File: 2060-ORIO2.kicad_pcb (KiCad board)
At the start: 4 copper layers, 100 x 100 mm, 196 parts, among them J11 RaspberryPI-B+header, J12 Conn_01x04, J13 Conn_01x08, J14 Conn_01x02, J15 Conn_01x08, J16 Conn_01x10, J17 Conn_01x10, J18 Conn_01x10, J19 Conn_01x10, J20 Conn_01x09, J21 Conn_01x08, J22 Conn_01x08, J23 Conn_01x08, J24 Conn_01x08, J25 Conn_01x08, J26 Conn_01x08, J27 Conn_01x02, J28 Conn_01x16, J29 Conn_01x16, J30 Conn_01x16, J31 Conn_01x08, J32 Conn_01x08, J33 Conn_01x08, J34 Conn_01x08, J35 TBL001-500-02GY-2GY, Q11 ULN2803ADWR, Q12 BCV27, SW11 SW_DIP_x08, U11 ICE40HX4K-TQ144, U12 SN74LVC4245AN, U13 SN74LVC4245AN, U14 SN74LVC4245AN, U15 TPS563231, U16 MCP3008, U17 AZ1117CH-3.3TRG1, U18 AZ1117CH-3.3TRG1, U19 AZ1117CH-1.2, U20 TPS563231, U21 SN74LVC4245AN, U22 SN74LVC4245AN, U23 SN74LVC4245AN, U24 SN74LVC4245AN, U25 TPS563231, U26 AP3012, Y11 XLH536025_000000I

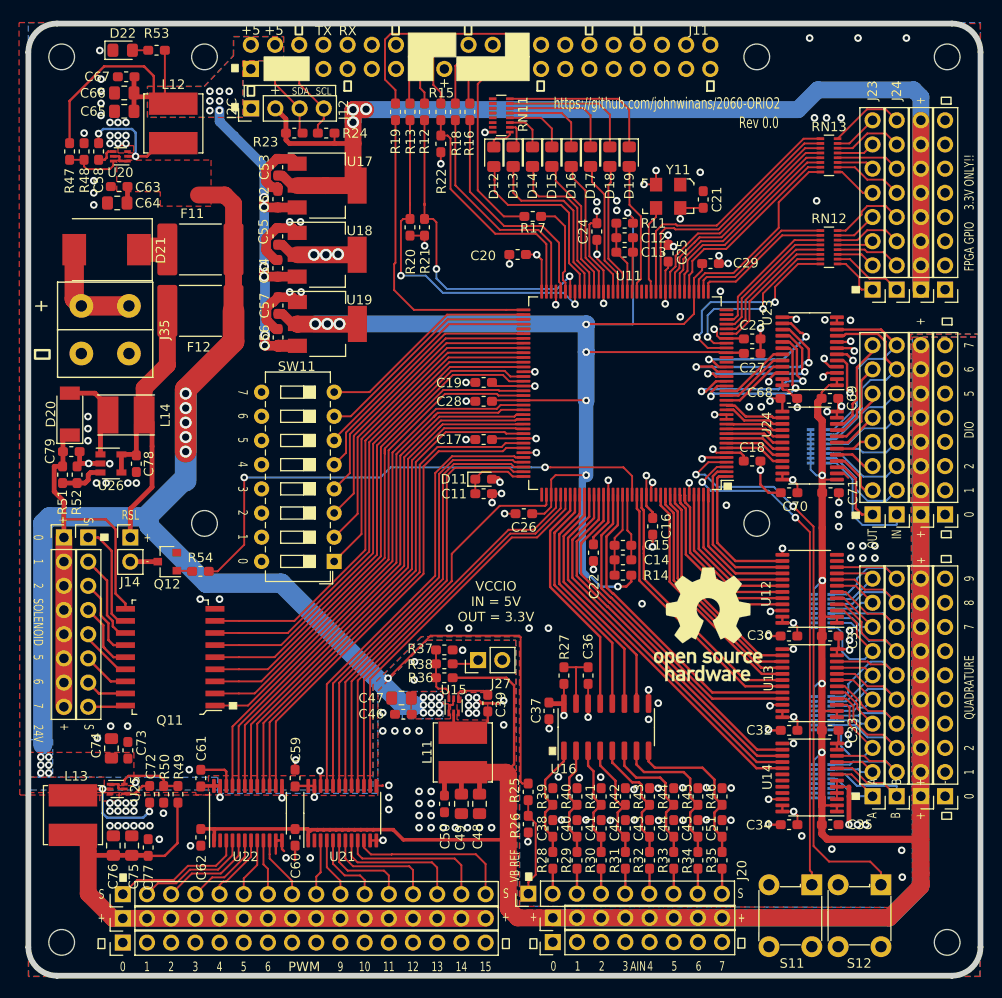
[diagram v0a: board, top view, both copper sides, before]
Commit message: Cosmetic silkscreen changes.
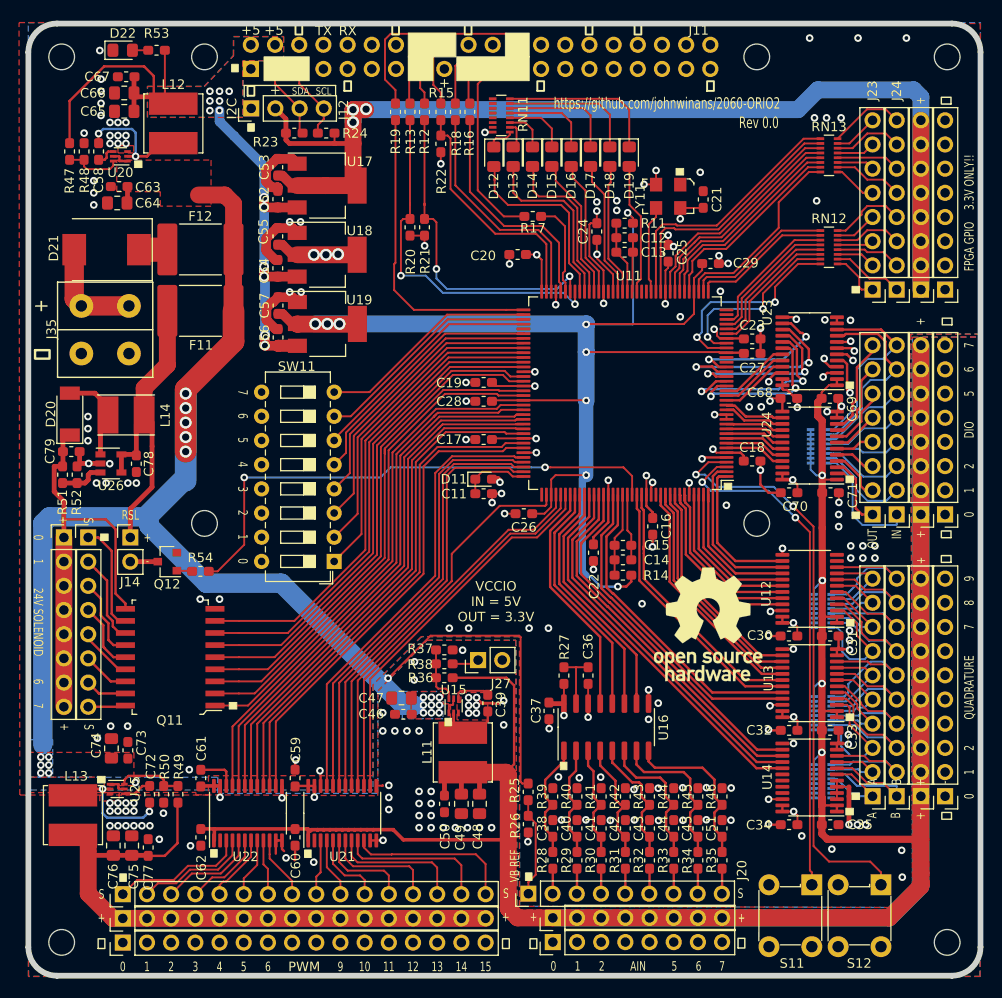
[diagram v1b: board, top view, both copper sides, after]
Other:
- board text added: "24V SOLENOID"
- board text removed: "24V"
- board text removed: "SOLENOID"
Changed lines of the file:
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@@
   (general
     (thickness 1.6)
-    (drawings 159)
+    (drawings 165)
     (tracks 2365)
     (zones 0)
@@
     (visible_elements FFFFFF7F)
     (pcbplotparams
-      (layerselection 0x010f8_ffffffff)
+      (layerselection 0x010f0_ffffffff)
       (usegerberextensions false)
       (usegerberattributes false)
@@
       (psa4output false)
       (plotreference true)
-      (plotvalue true)
+      (plotvalue false)
       (plotinvisibletext false)
       (padsonsilk false)
@@
     (tags "resistor handsolder")
     (attr smd)
-    (fp_text reference F12 (at 0.1778 -10.2616) (layer F.SilkS)
+    (fp_text reference F12 (at 0.0127 3.4798) (layer F.SilkS)
       (effects (font (size 1 1) (thickness 0.15)))
     )
@@
     (tags "resistor handsolder")
     (attr smd)
-    (fp_text reference F11 (at -0.8636 -10.2108) (layer F.SilkS)
+    (fp_text reference F11 (at 0.0508 3.6068) (layer F.SilkS)
       (effects (font (size 1 1) (thickness 0.15)))
     )
@@
     (tags "capacitor handsolder")
     (attr smd)
-    (fp_text reference C71 (at 2.3551 -0.0254 90) (layer F.SilkS)
+    (fp_text reference C71 (at 2.3297 0.2794 90) (layer F.SilkS)
       (effects (font (size 1 1) (thickness 0.15)))
     )
@@
     (tags "capacitor handsolder")
     (attr smd)
-    (fp_text reference C69 (at 2.3175 -0.0254 90) (layer F.SilkS)
+    (fp_text reference C69 (at 2.3175 1.1049 90) (layer F.SilkS)
       (effects (font (size 1 1) (thickness 0.15)))
     )
@@
     (tags "capacitor handsolder")
     (attr smd)
-    (fp_text reference C33 (at 2.3622 -0.0127 270) (layer F.SilkS)
+    (fp_text reference C33 (at 2.3241 0.6858 270) (layer F.SilkS)
       (effects (font (size 1 1) (thickness 0.15)))
     )
@@
     (tags "capacitor handsolder")
     (attr smd)
-    (fp_text reference C31 (at 2.3622 0.0381 90) (layer F.SilkS)
+    (fp_text reference C31 (at 2.3495 0.7493 90) (layer F.SilkS)
       (effects (font (size 1 1) (thickness 0.15)))
     )
@@
   (module jb-footprint:TBL001-500-02GY-2GY (layer F.Cu)
     (at 80.0658 74.1564 90)
-    (fp_text reference J35 (at 0 6.2484 270) (layer F.SilkS)
+    (fp_text reference J35 (at 0.0635 -5.6388 270) (layer F.SilkS)
       (effects (font (size 1 1) (thickness 0.15)))
     )
@@
     (tags "Diode SMC (DO-214AB)")
     (attr smd)
-    (fp_text reference D21 (at -5.6896 -0.0762 270) (layer F.SilkS)
+    (fp_text reference D21 (at 5.5499 0.1524 270) (layer F.SilkS)
       (effects (font (size 1 1) (thickness 0.15)))
     )
@@
     (at 140.467 59.018 180)
     (attr smd)
-    (fp_text reference Y11 (at 0.2286 1.651 180) (layer F.SilkS)
+    (fp_text reference Y11 (at 4.2037 -1.143 270) (layer F.SilkS)
       (effects (font (size 1 1) (thickness 0.15)))
     )
@@
     (tags "SOIC SO")
     (attr smd)
-    (fp_text reference U16 (at -4.3803 -4.4963 180) (layer F.SilkS)
+    (fp_text reference U16 (at -0.0369 6.0193 270) (layer F.SilkS)
       (effects (font (size 1 1) (thickness 0.15)))
     )
@@
     )
   )
+  (gr_poly (pts (xy 116.4528 114.9615) (xy 116.4528 115.7615) (xy 115.7528 115.7615) (xy 115.7528 114.9615)) (layer F.SilkS) (width 0.1))
+  (gr_poly (pts (xy 101.7081 128.7918) (xy 101.7081 129.5918) (xy 101.0081 129.5918) (xy 101.0081 128.7918)) (layer F.SilkS) (width 0.1))
+  (gr_poly (pts (xy 91.8402 128.7538) (xy 91.8402 129.5538) (xy 91.1402 129.5538) (xy 91.1402 128.7538)) (layer F.SilkS) (width 0.1))
+  (gr_poly (pts (xy 80.0658 121.7575) (xy 79.2658 121.7575) (xy 79.2658 121.0575) (xy 80.0658 121.0575)) (layer F.SilkS) (width 0.1))
+  (gr_poly (pts (xy 83.9393 57.1272) (xy 83.1393 57.1272) (xy 83.1393 56.4272) (xy 83.9393 56.4272)) (layer F.SilkS) (width 0.1))
+  (gr_poly (pts (xy 140.8226 57.9146) (xy 140.0226 57.9146) (xy 140.0226 57.2146) (xy 140.8226 57.2146)) (layer F.SilkS) (width 0.1))
+  (gr_poly (pts (xy 158.6534 125.1103) (xy 157.8534 125.1103) (xy 157.8534 124.4103) (xy 158.6534 124.4103)) (layer F.SilkS) (width 0.1))
+  (gr_poly (pts (xy 158.6788 115.2043) (xy 157.8788 115.2043) (xy 157.8788 114.5043) (xy 158.6788 114.5043)) (layer F.SilkS) (width 0.1))
+  (gr_poly (pts (xy 158.7169 105.2856) (xy 157.9169 105.2856) (xy 157.9169 104.5856) (xy 158.7169 104.5856)) (layer F.SilkS) (width 0.1))
+  (gr_poly (pts (xy 158.6661 90.2234) (xy 157.8661 90.2234) (xy 157.8661 89.5234) (xy 158.6661 89.5234)) (layer F.SilkS) (width 0.1))
+  (gr_poly (pts (xy 158.6788 80.3428) (xy 157.8788 80.3428) (xy 157.8788 79.6428) (xy 158.6788 79.6428)) (layer F.SilkS) (width 0.1))
   (gr_text RSL (at 82.7074 93.6382) (layer F.SilkS)
     (effects (font (size 1 0.7) (thickness 0.15)))
@@
   (gr_line (start 104.272 48.5024) (end 94.6708 48.5024) (layer F.SilkS) (width 0.12))
   (gr_line (start 104.272 49.5438) (end 104.272 48.5024) (layer F.SilkS) (width 0.12))
-  (gr_poly (pts (xy 94.05 50.382) (xy 94.05 51.182) (xy 93.35 51.182) (xy 93.35 50.382)) (layer F.SilkS) (width 0.1))
+  (gr_poly (pts (xy 95.7376 52.5157) (xy 95.7376 53.3157) (xy 95.0376 53.3157) (xy 95.0376 52.5157)) (layer F.SilkS) (width 0.1))
   (gr_text "Rev 0.0" (at 116.9212 53.3284) (layer B.SilkS)
     (effects (font (size 1.2 0.8) (thickness 0.2)) (justify mirror))
@@
     (effects (font (size 1.2 0.8) (thickness 0.2)) (justify mirror))
   )
-  (gr_text 24V (at 73.03 116.565 270) (layer F.SilkS)
-    (effects (font (size 1 0.7) (thickness 0.15)))
-  )
   (gr_poly (pts (xy 124.9 131.2) (xy 124.9 132) (xy 124.2 132) (xy 124.2 131.2)) (layer F.SilkS) (width 0.1))
   (gr_text 6 (at 94.5092 83.2153 270) (layer F.SilkS)
@@
   )
   (gr_poly (pts (xy 93.896 114) (xy 93.096 114) (xy 93.096 113.3) (xy 93.896 113.3)) (layer F.SilkS) (width 0.1))
-  (gr_poly (pts (xy 127.4 118) (xy 127.4 118.8) (xy 126.7 118.8) (xy 126.7 118)) (layer F.SilkS) (width 0.1))
-  (gr_poly (pts (xy 145.85 90.95) (xy 145.05 90.95) (xy 145.05 90.25) (xy 145.85 90.25)) (layer F.SilkS) (width 0.1))
+  (gr_poly (pts (xy 128.5686 119.5717) (xy 128.5686 120.3717) (xy 127.8686 120.3717) (xy 127.8686 119.5717)) (layer F.SilkS) (width 0.1))
+  (gr_poly (pts (xy 145.8772 90.9727) (xy 145.0772 90.9727) (xy 145.0772 90.2727) (xy 145.8772 90.2727)) (layer F.SilkS) (width 0.1))
   (gr_poly (pts (xy 94.05 46.28) (xy 94.05 47.08) (xy 93.35 47.08) (xy 93.35 46.28)) (layer F.SilkS) (width 0.1))
   (gr_poly (pts (xy 80.3854 96.3) (xy 79.5854 96.3) (xy 79.5854 95.6) (xy 80.3854 95.6)) (layer F.SilkS) (width 0.1))
@@
     (effects (font (size 1.016 1.016) (thickness 0.2032)))
   )
-  (gr_text 3 (at 134.7012 141.0092) (layer F.SilkS)
-    (effects (font (size 1 0.7) (thickness 0.15)))
-  )
   (gr_text 7 (at 144.8612 141.0092) (layer F.SilkS)
     (effects (font (size 1 0.7) (thickness 0.15)))
@@
     (effects (font (size 1 0.7) (thickness 0.15)))
   )
-  (gr_text 4 (at 137.3047 141.0092) (layer F.SilkS)
-    (effects (font (size 1 0.7) (thickness 0.15)))
-  )
   (gr_text 5 (at 139.8447 141.0092) (layer F.SilkS)
     (effects (font (size 1 0.7) (thickness 0.15)))
@@
     (effects (font (size 1 0.7) (thickness 0.15)))
   )
-  (gr_text 5 (at 73.03 108.5734 270) (layer F.SilkS)
-    (effects (font (size 1 0.7) (thickness 0.15)))
-  )
-  (gr_text SOLENOID (at 73.03 104.865 270) (layer F.SilkS)
-    (effects (font (size 1 0.7) (thickness 0.15)))
-  )
-  (gr_text 2 (at 73.03 101.055 270) (layer F.SilkS)
+  (gr_text "24V SOLENOID" (at 73.03 104.865 270) (layer F.SilkS)
     (effects (font (size 1 0.7) (thickness 0.15)))
   )
@@
   (segment (start 92.7895 120.5605) (end 92.602 120.373) (width 0.254) (layer F.Cu) (net 1))
   (segment (start 107.8955 127.7935) (end 108.5455 127.7935) (width 0.254) (layer F.Cu) (net 1))
-  (via (at 101.605 129.63) (size 0.8) (drill 0.4) (layers F.Cu B.Cu) (net 1))
+  (via (at 101.9733 130.0745) (size 0.8) (drill 0.4) (layers F.Cu B.Cu) (net 1))
   (segment (start 100.0175 128.9175) (end 100.0175 129.8205) (width 0.254) (layer F.Cu) (net 1))
   (segment (start 100.0175 129.8205) (end 99.954 129.884) (width 0.254) (layer F.Cu) (net 1))

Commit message: Change regulators & add current limiters.
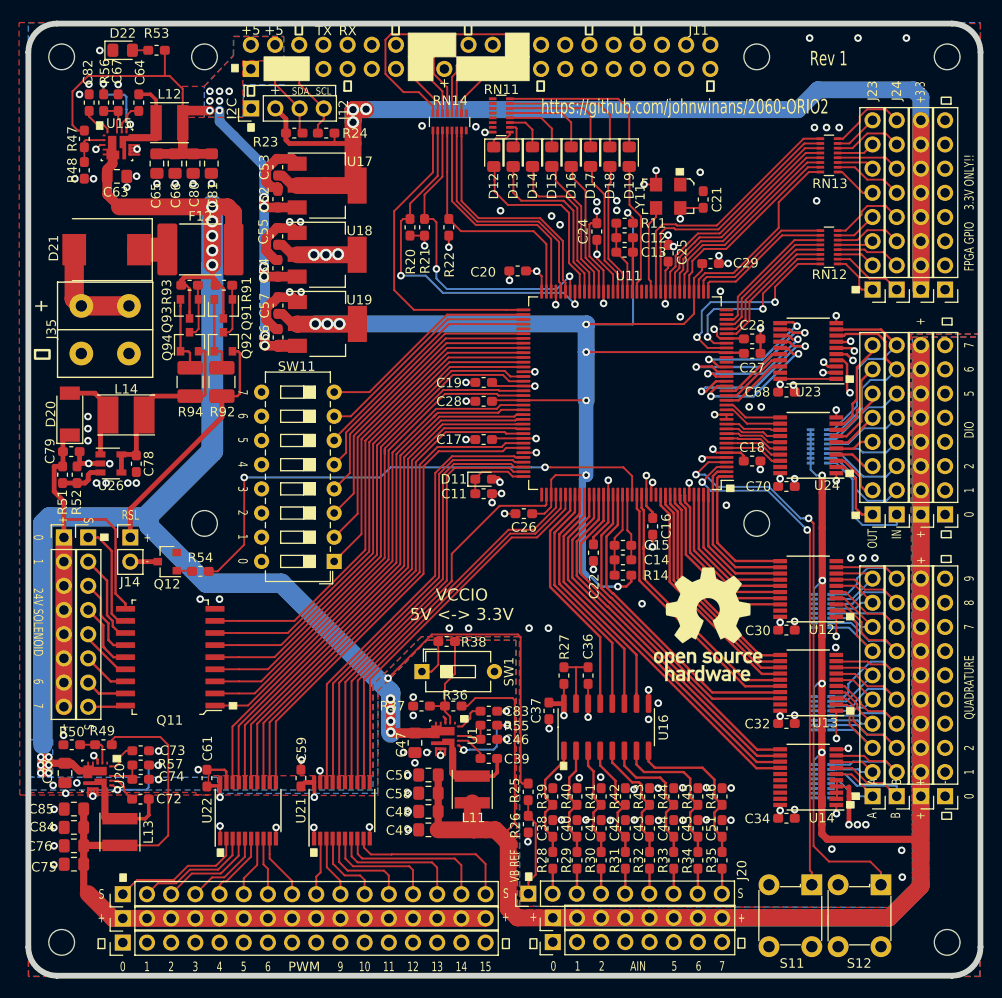
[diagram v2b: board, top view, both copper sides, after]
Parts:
- removed C31, C33, C35, C60, C62, C69, C71: .1uF, Capacitor_SMD:C_0603_1608Metric_Pad1.05x0.95mm_HandSolder
- removed F11: .5A, Fuse:Fuse_2920_7451Metric_Pad2.10x5.45mm_HandSolder
- removed J27: Conn_01x02, Connector_PinHeader_2.54mm:PinHeader_1x02_P2.54mm_Vertical
- removed the LOGO11 at (125.6, 58.3)
- removed R12, R13, R15, R16, R17, R18, R19: 33, Resistor_SMD:R_0603_1608Metric_Pad1.05x0.95mm_HandSolder
- removed U25: TPS563231, jb-footprint:SOT-563
- added C80: 22uF, Capacitor_SMD:C_0805_2012Metric_Pad1.15x1.40mm_HandSolder, F.Cu at (89.3, 56.7)
- added C81: 22uF, Capacitor_SMD:C_0805_2012Metric_Pad1.15x1.40mm_HandSolder, F.Cu at (91.2, 56.7)
- added C82: .001uF, Capacitor_SMD:C_0603_1608Metric_Pad1.05x0.95mm_HandSolder, F.Cu at (78.4, 50.3)
- added C83: .001uF, Capacitor_SMD:C_0603_1608Metric_Pad1.05x0.95mm_HandSolder, F.Cu at (120.4, 114.2)
- added C84: 22uF, Capacitor_SMD:C_0805_2012Metric_Pad1.15x1.40mm_HandSolder, F.Cu at (76.8, 126.4)
- added C85: 22uF, Capacitor_SMD:C_0805_2012Metric_Pad1.15x1.40mm_HandSolder, F.Cu at (76.8, 124.5)
- added Q91: BCV27, Package_TO_SOT_SMD:SOT-23, F.Cu at (92.5, 72.0)
- added Q92: BCV27, Package_TO_SOT_SMD:SOT-23, F.Cu at (92.5, 75.4)
- added Q93: BCV27, Package_TO_SOT_SMD:SOT-23, F.Cu at (88.9, 72.0)
- added Q94: BCV27, Package_TO_SOT_SMD:SOT-23, F.Cu at (88.9, 75.4)
- added R55: x, Resistor_SMD:R_0603_1608Metric_Pad1.05x0.95mm_HandSolder, F.Cu at (120.4, 115.7)
- added R56: x, Resistor_SMD:R_0603_1608Metric_Pad1.05x0.95mm_HandSolder, F.Cu at (79.9, 50.3)
- added R57: x, Resistor_SMD:R_0603_1608Metric_Pad1.05x0.95mm_HandSolder, F.Cu at (83.8, 119.9)
- added R91: 10K, Resistor_SMD:R_0603_1608Metric_Pad1.05x0.95mm_HandSolder, F.Cu at (92.5, 69.5)
- added R92: 1.2, Resistor_SMD:R_1210_3225Metric_Pad1.42x2.65mm_HandSolder, F.Cu at (92.3, 79.6)
- added R93: 10K, Resistor_SMD:R_0603_1608Metric_Pad1.05x0.95mm_HandSolder, F.Cu at (88.9, 69.5)
- added R94: 1.2, Resistor_SMD:R_1210_3225Metric_Pad1.42x2.65mm_HandSolder, F.Cu at (89.0, 79.6)
- added RN14: 33, Resistor_SMD:R_Array_Convex_8x0602, F.Cu at (116.2, 52.3)
- added SW1: SW_DIP_x01, Button_Switch_THT:SW_DIP_SPSTx01_Slide_6.7x4.1mm_W7.62mm_P2.54mm_LowProfile, F.Cu at (113.3, 110.1)
- added U1: AOZ2151TQI-19, jb-footprint:AOZ2151TQI-19, F.Cu at (115.8, 116.8)
- C46, C67: value .1uF -> 4.7uF
- C47: value 10uF -> 22uF
- C50, C58, C63, C77: value .1uF -> 22uF; footprint Capacitor_SMD:C_0603_1608Metric_Pad1.05x0.95mm_HandSolder -> Capacitor_SMD:C_0805_2012Metric_Pad1.15x1.40mm_HandSolder
- C64: value 10uF -> .1uF; footprint Capacitor_SMD:C_0805_2012Metric_Pad1.15x1.40mm_HandSolder -> Capacitor_SMD:C_0603_1608Metric_Pad1.05x0.95mm_HandSolder
- C73: value .1uF -> .001uF
- C74: value 10uF -> 4.7uF; footprint Capacitor_SMD:C_0805_2012Metric_Pad1.15x1.40mm_HandSolder -> Capacitor_SMD:C_0603_1608Metric_Pad1.05x0.95mm_HandSolder
- F12: value Polyfuse -> 6A
- L11, L12, L13: value 4.7uH -> 2.2uH; footprint Inductor_SMD:L_Bourns_SRN6045TA -> Inductor_SMD:L_Taiyo-Yuden_MD-4040
- R27: value 2K2 -> 100
- R36: value 45K3 -> x
- R37, R48, R50: value 10K -> x
- R38: value 16K2 -> x
- R47: value 73K2 -> x
- R49: value 90K -> x
- U12, U13, U14, U21, U22, U23, U24: value SN74LVC4245AN -> ‎74LVT245B; footprint Package_SO:TSSOP-24_4.4x7.8mm_P0.65mm -> Package_SO:TSSOP-20_4.4x6.5mm_P0.65mm
- U15, U20: value TPS563231 -> AOZ2151TQI-19; footprint jb-footprint:SOT-563 -> jb-footprint:AOZ2151TQI-19
- moved C58 75.8 mm to (114.0, 122.8), turned to 180 degrees
- moved U15 68.7 mm to (81.3, 54.8), turned to 0 degrees
- moved U20 65.1 mm to (79.3, 121.0), turned to 270 degrees
- moved C77 11.7 mm to (75.8, 120.7), turned to 270 degrees
- moved R50 11.0 mm to (76.6, 117.7), turned to 180 degrees
- moved C64 10.8 mm to (83.6, 50.3), turned to 90 degrees
- moved R49 9.40 mm to (79.9, 117.7), turned to 180 degrees
- moved C46 9.36 mm to (120.4, 117.2), turned to 0 degrees
- moved C66 9.14 mm to (87.4, 56.7), turned to 270 degrees
- moved R22 8.80 mm to (116.2, 63.4)
- moved C65 6.47 mm to (85.5, 56.7), turned to 270 degrees
- moved C75 6.38 mm to (76.8, 130.3), turned to 180 degrees
- moved R37 6.36 mm to (113.3, 113.7), turned to 180 degrees
- moved C39 5.82 mm to (120.4, 119.2), turned to 0 degrees
- moved C48 5.43 mm to (114.0, 124.8), turned to 180 degrees
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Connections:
- C46 pad 1: +BATT -> Net-(C46-Pad1)
- C58 pad 1: Net-(C58-Pad1) -> VCC_IO
- C58 pad 2: Net-(C58-Pad2) -> GND
- C64 pad 1: +BATT -> Net-(C64-Pad1)
- C64 pad 2: GND -> Net-(C64-Pad2)
- C67 pad 1: 5V_PI -> Net-(C67-Pad1)
- C73 pad 1: +BATT -> Net-(C73-Pad1)
- C74 pad 1: +BATT -> Net-(C74-Pad1)
- C77 pad 1: VCC_PWM -> +BATT
- C78 pad 1: VCC_SOL_12 -> /VB_RSOL
- J14 pad 1: VCC_SOL_12 -> /VB_RSL
- L12 pad 1: Net-(C58-Pad2) -> Net-(C64-Pad2)
- L14 pad 1: VCC_SOL_12 -> /VB_RSOL
- U12 pad 1: VCC_IO -> +3V3
- U12 pad 10: /QB9 -> GND
- U12 pad 11: GND -> /FPGA_QB9
- U12 pad 12: GND -> /FPGA_QA9
- U12 pad 13: GND -> /FPGA_QB8
- U12 pad 14: /FPGA_QB9 -> /FPGA_QA8
- U12 pad 15: /FPGA_QA9 -> /FPGA_QB7
- U12 pad 16: /FPGA_QB8 -> /FPGA_QA7
- U12 pad 17: /FPGA_QA8 -> /FPGA_QB6
- U12 pad 18: /FPGA_QB7 -> /FPGA_QA6
- U12 pad 19: /FPGA_QA7 -> GND
- U12 pad 2: VCC_IO -> /QA6
- U12 pad 20: /FPGA_QB6 -> +3V3
- U12 pad 3: /QA6 -> /QB6
- U12 pad 4: /QB6 -> /QA7
- U12 pad 5: /QA7 -> /QB7
- U12 pad 6: /QB7 -> /QA8
- U12 pad 7: /QA8 -> /QB8
- U12 pad 8: /QB8 -> /QA9
- U12 pad 9: /QA9 -> /QB9
- U13 pad 1: VCC_IO -> +3V3
- U13 pad 10: /QB5 -> GND
- U13 pad 11: GND -> /FPGA_QB5
- U13 pad 12: GND -> /FPGA_QA5
- U13 pad 13: GND -> /FPGA_QB4
- U13 pad 14: /FPGA_QB5 -> /FPGA_QA4
- U13 pad 15: /FPGA_QA5 -> /FPGA_QB3
- U13 pad 16: /FPGA_QB4 -> /FPGA_QA3
- U13 pad 17: /FPGA_QA4 -> /FPGA_QB2
- U13 pad 18: /FPGA_QB3 -> /FPGA_QA2
- U13 pad 19: /FPGA_QA3 -> GND
- U13 pad 2: VCC_IO -> /QA2
- U13 pad 20: /FPGA_QB2 -> +3V3
- U13 pad 3: /QA2 -> /QB2
- U13 pad 4: /QB2 -> /QA3
- U13 pad 5: /QA3 -> /QB3
- U13 pad 6: /QB3 -> /QA4
- U13 pad 7: /QA4 -> /QB4
- U13 pad 8: /QB4 -> /QA5
- U13 pad 9: /QA5 -> /QB5
- U14 pad 1: VCC_IO -> +3V3
- U14 pad 10: /QB1 -> GND
- U14 pad 11: GND -> /FPGA_QB1
- U14 pad 12: GND -> /FPGA_QA1
- U14 pad 13: GND -> /FPGA_QB0
- U14 pad 14: /FPGA_QB1 -> /FPGA_QA0
- U14 pad 15: /FPGA_QA1 -> Net-(U14-Pad15)
- U14 pad 16: /FPGA_QB0 -> Net-(U14-Pad16)
- U14 pad 17: /FPGA_QA0 -> Net-(U14-Pad17)
- U14 pad 19: Net-(U14-Pad19) -> GND
- U14 pad 2: VCC_IO -> Net-(NT1-Pad2)
- U14 pad 20: Net-(U14-Pad20) -> +3V3
- U14 pad 6: Net-(NT1-Pad2) -> /QA0
- U14 pad 7: /QA0 -> /QB0
- U14 pad 8: /QB0 -> /QA1
- U14 pad 9: /QA1 -> /QB1
- U15 pad 1: +BATT -> Net-(U15-Pad1)
- U15 pad 2: Net-(C39-Pad2) -> Net-(R47-Pad2)
- U15 pad 4: Net-(C39-Pad1) -> +BATT
- U20 pad 1: +BATT -> Net-(U20-Pad1)
- U20 pad 2: Net-(C58-Pad2) -> Net-(R49-Pad2)
- U20 pad 4: Net-(C58-Pad1) -> +BATT
- U21 pad 1: VCC_IO -> GND
- U21 pad 10: /PWM15 -> GND
- U21 pad 11: GND -> /FPGA_PWM15
- U21 pad 12: GND -> /FPGA_PWM14
- U21 pad 13: GND -> /FPGA_PWM13
- U21 pad 14: /FPGA_PWM15 -> /FPGA_PWM12
- U21 pad 15: /FPGA_PWM14 -> /FPGA_PWM11
- U21 pad 16: /FPGA_PWM13 -> /FPGA_PWM10
- U21 pad 17: /FPGA_PWM12 -> /FPGA_PWM9
- U21 pad 18: /FPGA_PWM11 -> /FPGA_PWM8
- U21 pad 19: /FPGA_PWM10 -> GND
- U21 pad 2: GND -> /PWM8
- U21 pad 20: /FPGA_PWM9 -> +3V3
- U21 pad 3: /PWM8 -> /PWM9
- U21 pad 4: /PWM9 -> /PWM10
- U21 pad 5: /PWM10 -> /PWM11
- U21 pad 6: /PWM11 -> /PWM12
- U21 pad 7: /PWM12 -> /PWM13
- U21 pad 8: /PWM13 -> /PWM14
- U21 pad 9: /PWM14 -> /PWM15
- U22 pad 1: VCC_IO -> GND
- U22 pad 10: /PWM7 -> GND
- U22 pad 11: GND -> /FPGA_PWM7
- U22 pad 12: GND -> /FPGA_PWM6
- U22 pad 13: GND -> /FPGA_PWM5
- U22 pad 14: /FPGA_PWM7 -> /FPGA_PWM4
- U22 pad 15: /FPGA_PWM6 -> /FPGA_PWM3
- U22 pad 16: /FPGA_PWM5 -> /FPGA_PWM2
- U22 pad 17: /FPGA_PWM4 -> /FPGA_PWM1
- U22 pad 18: /FPGA_PWM3 -> /FPGA_PWM0
- U22 pad 19: /FPGA_PWM2 -> GND
- U22 pad 2: GND -> /PWM0
- U22 pad 20: /FPGA_PWM1 -> +3V3
- U22 pad 3: /PWM0 -> /PWM1
- U22 pad 4: /PWM1 -> /PWM2
- U22 pad 5: /PWM2 -> /PWM3
- U22 pad 6: /PWM3 -> /PWM4
- U22 pad 7: /PWM4 -> /PWM5
- U22 pad 8: /PWM5 -> /PWM6
- U22 pad 9: /PWM6 -> /PWM7
- U23 pad 1: VCC_IO -> +3V3
- U23 pad 10: /DIN7 -> GND
- U23 pad 11: GND -> /FPGA_DIN7
- U23 pad 12: GND -> /FPGA_DIN6
- U23 pad 13: GND -> /FPGA_DIN5
- U23 pad 14: /FPGA_DIN7 -> /FPGA_DIN4
- U23 pad 15: /FPGA_DIN6 -> /FPGA_DIN3
- U23 pad 16: /FPGA_DIN5 -> /FPGA_DIN2
- U23 pad 17: /FPGA_DIN4 -> /FPGA_DIN1
- U23 pad 18: /FPGA_DIN3 -> /FPGA_DIN0
- U23 pad 19: /FPGA_DIN2 -> GND
- U23 pad 2: VCC_IO -> /DIN0
- U23 pad 20: /FPGA_DIN1 -> +3V3
- U23 pad 3: /DIN0 -> /DIN1
- U23 pad 4: /DIN1 -> /DIN2
- U23 pad 5: /DIN2 -> /DIN3
- U23 pad 6: /DIN3 -> /DIN4
- U23 pad 7: /DIN4 -> /DIN5
- U23 pad 8: /DIN5 -> /DIN6
- U23 pad 9: /DIN6 -> /DIN7
- U24 pad 1: VCC_IO -> GND
- U24 pad 10: /DOUT7 -> GND
- U24 pad 11: GND -> /FPGA_DOUT7
- U24 pad 12: GND -> /FPGA_DOUT6
- U24 pad 13: GND -> /FPGA_DOUT5
- U24 pad 14: /FPGA_DOUT7 -> /FPGA_DOUT4
- U24 pad 15: /FPGA_DOUT6 -> /FPGA_DOUT3
- U24 pad 16: /FPGA_DOUT5 -> /FPGA_DOUT2
- U24 pad 17: /FPGA_DOUT4 -> /FPGA_DOUT1
- U24 pad 18: /FPGA_DOUT3 -> /FPGA_DOUT0
- U24 pad 19: /FPGA_DOUT2 -> GND
- U24 pad 2: GND -> /DOUT0
- U24 pad 20: /FPGA_DOUT1 -> +3V3
- U24 pad 3: /DOUT0 -> /DOUT1
- U24 pad 4: /DOUT1 -> /DOUT2
- U24 pad 5: /DOUT2 -> /DOUT3
- U24 pad 6: /DOUT3 -> /DOUT4
- U24 pad 7: /DOUT4 -> /DOUT5
- U24 pad 8: /DOUT5 -> /DOUT6
- U24 pad 9: /DOUT6 -> /DOUT7
- U26 pad 4: VCC_SOL_12 -> /VB_RSOL
- U26 pad 5: VCC_SOL_12 -> /VB_RSOL
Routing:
- net VCC_IO: track 368.4 -> 314.0 mm
- net +BATT: track 157.4 -> 204.5 mm, vias 21 -> 16
- net VCC_SOL_12: track 33.2 -> 0.00 mm
- net /VB_RSL: track 0.00 -> 25.9 mm
- net /VB_RSOL: track 0.00 -> 21.3 mm
- net GND: track 130.4 -> 112.0 mm, vias 201 -> 155
- net /FPGA_SDO: track 10.0 -> 25.2 mm
- net /SPI_MISO: track 19.4 -> 6.02 mm
- net Net-(C58-Pad2): track 13.1 -> 0.00 mm, vias 2 -> 0
- net VCC_PWM: track 64.6 -> 77.6 mm
- net Net-(C64-Pad2): track 0.00 -> 11.4 mm
- net +3V3: track 162.5 -> 172.2 mm, vias 23 -> 26
- net Net-(R55-Pad2): track 0.00 -> 8.63 mm, vias 0 -> 2
- net Net-(R56-Pad2): track 0.00 -> 8.63 mm, vias 0 -> 2
- net Net-(R57-Pad2): track 0.00 -> 8.42 mm, vias 0 -> 2
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- added copper zone on In2.Cu, net 5V_PI
- removed copper zone on F.Cu, net +BATT
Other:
- rule pad_to_mask_clearance: 0.051 -> 0.0254
- rule solder_mask_min_width: 0.25 -> 0.0254
- board text added: "+3.3"
- board text added: "Rev 1"
- board text added: "VCCIO 5V <-> 3.3V"
- board text removed: "Rev 0.0"
- board text removed: "VCCIO IN = 5V OUT = 3.3V"
